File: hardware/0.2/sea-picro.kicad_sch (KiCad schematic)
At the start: 56 parts, among them J1 USB_C_Receptacle_USB2.0, J2 0.1" x 12, J3 0.1" x 12, Q1 FDG6335N, Q2 FDG6335N, SW1 RESET, U1 AP2112K-3.3, U3 W25Q128JVPIQ, U4 RP2040, Y1 12MHz

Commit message: 0.2 ready for review
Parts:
- added LOGO2: Sea-Picro, josh-logos:sea-picro-silk, symbol Graphic:SYM_LASER_Small
- added R6: 5K1, Resistor_SMD:R_0402_1005Metric, symbol Device:R
- C1, C10, C11, C12, C13, C14, C15, C16, C17, C18, C2, C3, C4, C8, C9, R1, R11, R12, R15, R2, R3, R4, R5, R9: JLC Basic (none) -> Y
- C19, C5: JLC Basic (none) -> Y; LCSC (none) -> C23733; MPN  (none) -> CL05A475MP5NRNC; Manufacturer (none) -> Samsung Electro-Mechanics
- C6, C7: JLC Basic (none) -> Y; LCSC C14445 -> C1548; MPN  CL05A105KP5NNNC -> 0402CG150J500NT; Manufacturer Samsung Electro-Mechanics -> FH(Guangdong Fenghua Advanced Tech)
- D1: JLC Basic (none) -> N; LCSC C699102 -> C122854; Manufacturer Yangzhou Yangjie Elec Tech -> Shikues
- D2: JLC Basic (none) -> Y; LCSC C268294 -> C72041; MPN  OSK40603C1E -> 19-217/BHC-ZL1M2RY/3T; Manufacturer OptoSupplyr -> Everlight Elec
- D3, F1, J1, R7, R8: JLC Basic (none) -> N
- Q1, Q2: value FDG6335N -> 2N7002DW-7-F; JLC Basic (none) -> N; LCSC (none) -> C83571; MPN  (none) -> 2N7002DW-7-F; Manufacturer (none) -> Diodes Incorporated
- R10: value 10K -> 5K1; JLC Basic (none) -> Y
- R13: JLC Basic (none) -> Y; LCSC (none) -> C25794; MPN  (none) -> 0402WGF5102TCE; Manufacturer (none) -> UNI-ROYAL(Uniroyal Elec)
- R14: JLC Basic (none) -> Y; LCSC (none) -> C25905; MPN  (none) -> 0402WGF5101TCE; Manufacturer (none) -> UNI-ROYAL(Uniroyal Elec)
- SW1: JLC Basic (none) -> N; LCSC (none) -> C913778; MPN  (none) -> 1TS026A-1000-0550-CT; Manufacturer (none) -> HYP (Hongyuan Precision)
- U1: value AP2112K-3.3 -> ME6211C33M5G-N; JLC Basic (none) -> N; LCSC C51118 -> C82942; MPN  AP2112K-3.3TRG1 -> ME6211C33M5G-N; Manufacturer Diodes Incorporated -> MICRONE(Nanjing Micro One Elec)
- U2: renamed from U3; value W25Q128JVPIQ -> GD25Q64CWIGR; JLC Basic (none) -> N; LCSC C190862 -> C395511; MPN  W25Q128JVPIQ -> GD25Q64CWIGR; Manufacturer Winbond Elec -> GigaDevice
- U3: renamed from U4; JLC Basic (none) -> N
- Y1: JLC Basic (none) -> Y; LCSC (none) -> C9002; MPN  (none) -> X322512MSB4SI; Manufacturer (none) -> Yangxing Tech
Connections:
- net +3V3: now also R6.1; no longer R10.1
- new net: R10.1, R6.2
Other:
- note added: "Q1A - inverter, as button can only pull to ground due to being backwards compatiable"
- note added: "Q1B - using body diode due to lack of space. Can sub with normal diode"
- note added: "Q2A - pulls nRST to GND"
- note removed: "Q1A - inverter, as button can only pull to ground"
- note removed: "Q1B - pulls nRST to GND"
- note removed: "Q2A - using body diode due to lack of space. Can sub with normal diode"

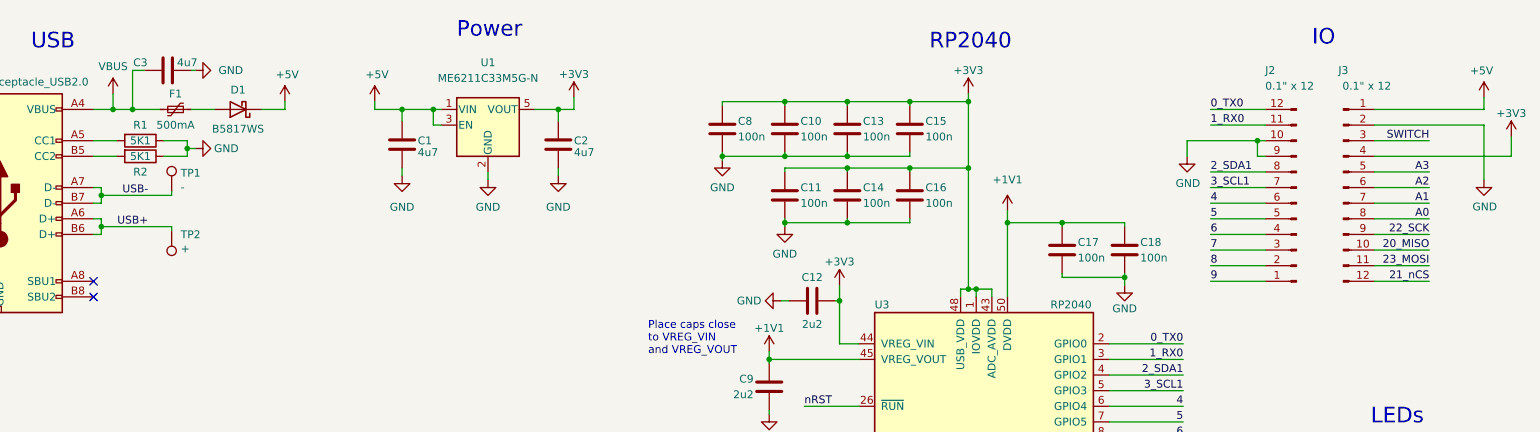
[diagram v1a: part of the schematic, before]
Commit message: add USB D+- on pin header
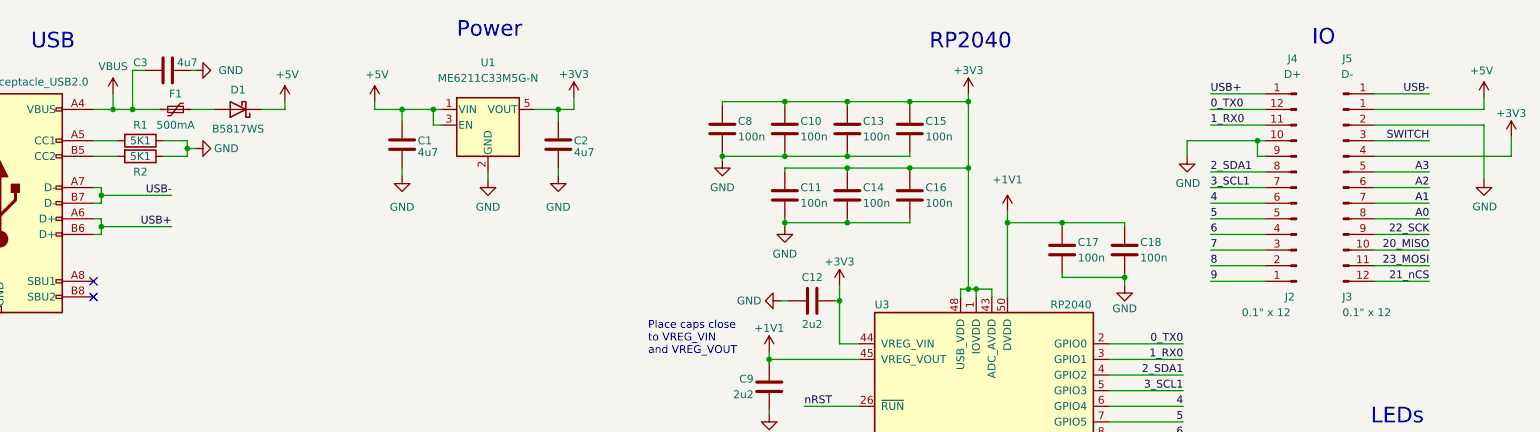
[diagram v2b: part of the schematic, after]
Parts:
- removed TP1: -, TestPoint:TestPoint_Pad_D1.0mm, symbol Connector:TestPoint
- removed TP2: +, TestPoint:TestPoint_Pad_D1.0mm, symbol Connector:TestPoint
- added J4: D+, josh-connectors:PinHeader_1x01_Circle, symbol Connector:Conn_01x01_Male
- added J5: D-, josh-connectors:PinHeader_1x01_Circle, symbol Connector:Conn_01x01_Male
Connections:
- net USB+: now also J4.1 (Pin_1)
- net USB-: now also J5.1 (Pin_1)
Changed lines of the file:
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@@
     (stroke (width 0) (type default) (color 0 0 0 0))
   )
+  (wire (pts (xy 231.14 28.575) (xy 240.03 28.575))
+    (stroke (width 0) (type default) (color 0 0 0 0))
+  )
   (wire (pts (xy 231.14 43.815) (xy 240.03 43.815))
     (stroke (width 0) (type default) (color 0 0 0 0))
@@
     (stroke (width 0) (type default) (color 0 0 0 0))
   )
-  (wire (pts (xy 62.23 44.45) (xy 62.23 45.085))
-    (stroke (width 0) (type default) (color 0 0 0 0))
-  )
   (wire (pts (xy 22.86 185.42) (xy 24.765 185.42))
     (stroke (width 0) (type default) (color 0 0 0 0))
@@
     (stroke (width 0) (type default) (color 0 0 0 0))
   )
+  (wire (pts (xy 257.81 28.575) (xy 266.7 28.575))
+    (stroke (width 0) (type default) (color 0 0 0 0))
+  )
   (wire (pts (xy 114.3 168.275) (xy 121.92 168.275))
     (stroke (width 0) (type default) (color 0 0 0 0))
@@
     (stroke (width 0) (type default) (color 0 0 0 0))
   )
-  (wire (pts (xy 62.23 50.8) (xy 62.23 50.165))
-    (stroke (width 0) (type default) (color 0 0 0 0))
-  )
   (wire (pts (xy 170.815 59.69) (xy 170.815 62.23))
     (stroke (width 0) (type default) (color 0 0 0 0))
@@
     (effects (font (size 1.27 1.27)) (justify right bottom))
   )
-  (label "USB-" (at 58.42 45.085 180)
+  (label "USB-" (at 62.23 45.085 180)
     (effects (font (size 1.27 1.27)) (justify right bottom))
   )
@@
     (effects (font (size 1.27 1.27)) (justify left bottom))
   )
+  (label "USB-" (at 266.7 28.575 180)
+    (effects (font (size 1.27 1.27)) (justify right bottom))
+  )
   (label "2_SDA1" (at 231.14 41.275 0)
     (effects (font (size 1.27 1.27)) (justify left bottom))
@@
     (effects (font (size 1.27 1.27)) (justify left bottom))
   )
+  (label "USB+" (at 231.14 28.575 0)
+    (effects (font (size 1.27 1.27)) (justify left bottom))
+  )
   (label "22_SCK" (at 266.7 51.435 180)
     (effects (font (size 1.27 1.27)) (justify right bottom))
@@
     (effects (font (size 1.27 1.27)) (justify left bottom))
   )
-  (label "USB+" (at 58.42 50.165 180)
+  (label "USB+" (at 62.23 50.165 180)
     (effects (font (size 1.27 1.27)) (justify right bottom))
   )
@@
   (symbol (lib_id "Connector:Conn_01x12_Male") (at 245.11 46.355 180) (unit 1)
     (in_bom no) (on_board yes)
-    (property "Reference" "J2" (id 0) (at 240.03 24.765 0)
+    (property "Reference" "J2" (id 0) (at 243.205 61.595 0)
       (effects (font (size 1.27 1.27)) (justify right))
     )
-    (property "Value" "0.1\" x 12" (id 1) (at 240.03 27.305 0)
+    (property "Value" "0.1\" x 12" (id 1) (at 236.22 64.135 0)
       (effects (font (size 1.27 1.27)) (justify right))
     )
@@
   (symbol (lib_id "Connector:Conn_01x12_Male") (at 252.73 43.815 0) (unit 1)
     (in_bom no) (on_board yes)
-    (property "Reference" "J3" (id 0) (at 252.73 24.765 0))
-    (property "Value" "0.1\" x 12" (id 1) (at 256.54 27.305 0))
+    (property "Reference" "J3" (id 0) (at 253.365 61.595 0))
+    (property "Value" "0.1\" x 12" (id 1) (at 256.54 64.135 0))
     (property "Footprint" "josh-connectors:Castellated_Short_P2.54x12" (id 2) (at 252.73 43.815 0)
       (effects (font (size 1.27 1.27)) hide)
@@
     )
   )
-  (symbol (lib_id "Connector:TestPoint") (at 62.23 44.45 0) (unit 1)
-    (in_bom no) (on_board yes)
-    (property "Reference" "TP1" (id 0) (at 63.7032 41.4528 0)
-      (effects (font (size 1.27 1.27)) (justify left))
-    )
-    (property "Value" "-" (id 1) (at 63.7032 43.7642 0)
-      (effects (font (size 1.27 1.27)) (justify left))
-    )
-    (property "Footprint" "TestPoint:TestPoint_Pad_D1.0mm" (id 2) (at 67.31 44.45 0)
-      (effects (font (size 1.27 1.27)) hide)
-    )
-    (property "Datasheet" "~" (id 3) (at 67.31 44.45 0)
-      (effects (font (size 1.27 1.27)) hide)
-    )
-    (property "DNP" "DNP" (id 4) (at 62.23 44.45 0)
-      (effects (font (size 1.27 1.27)) hide)
-    )
-    (pin "1")
-  )
-  (symbol (lib_id "Connector:TestPoint") (at 62.23 50.8 180) (unit 1)
-    (in_bom no) (on_board yes)
-    (property "Reference" "TP2" (id 0) (at 63.7032 51.4604 0)
-      (effects (font (size 1.27 1.27)) (justify right))
-    )
-    (property "Value" "+" (id 1) (at 63.7032 53.7718 0)
-      (effects (font (size 1.27 1.27)) (justify right))
-    )
-    (property "Footprint" "TestPoint:TestPoint_Pad_D1.0mm" (id 2) (at 57.15 50.8 0)
-      (effects (font (size 1.27 1.27)) hide)
-    )
-    (property "Datasheet" "~" (id 3) (at 57.15 50.8 0)
-      (effects (font (size 1.27 1.27)) hide)
-    )
-    (property "DNP" "DNP" (id 4) (at 62.23 50.8 0)
-      (effects (font (size 1.27 1.27)) hide)
-    )
-    (pin "1")
-  )
   (symbol (lib_id "Device:C") (at 159.385 76.2 0) (mirror y) (unit 1)
     (in_bom yes) (on_board yes)
@@
     (pin "2")
   )
+  (symbol (lib_id "Connector:Conn_01x01_Male") (at 245.11 28.575 180) (unit 1)
+    (in_bom yes) (on_board yes) (fields_autoplaced)
+    (property "Reference" "J4" (id 0) (at 244.475 22.86 0))
+    (property "Value" "D+" (id 1) (at 244.475 25.4 0))
+    (property "Footprint" "josh-connectors:PinHeader_1x01_Circle" (id 2) (at 245.11 28.575 0)
+      (effects (font (size 1.27 1.27)) hide)
+    )
+    (property "Datasheet" "~" (id 3) (at 245.11 28.575 0)
+      (effects (font (size 1.27 1.27)) hide)
+    )
+    (pin "1")
+  )
   (symbol (lib_id "power:+1V1") (at 159.385 70.485 0) (unit 1)
     (in_bom yes) (on_board yes)
@@
     (pin "1")
   )
+  (symbol (lib_id "Connector:Conn_01x01_Male") (at 252.73 28.575 0) (unit 1)
+    (in_bom yes) (on_board yes) (fields_autoplaced)
+    (property "Reference" "J5" (id 0) (at 253.365 22.86 0))
+    (property "Value" "D-" (id 1) (at 253.365 25.4 0))
+    (property "Footprint" "josh-connectors:PinHeader_1x01_Circle" (id 2) (at 252.73 28.575 0)
+      (effects (font (size 1.27 1.27)) hide)
+    )
+    (property "Datasheet" "~" (id 3) (at 252.73 28.575 0)
+      (effects (font (size 1.27 1.27)) hide)
+    )
+    (pin "1")
+  )
   (symbol (lib_id "Connector:TestPoint") (at 166.37 118.745 90) (unit 1)
     (in_bom no) (on_board yes)
@@
       (reference "J3") (unit 1) (value "0.1\" x 12") (footprint "josh-connectors:Castellated_Short_P2.54x12")
     )
+    (path "/6c8fe750-f5d5-45e3-8031-75f1034c352b"
+      (reference "J4") (unit 1) (value "D+") (footprint "josh-connectors:PinHeader_1x01_Circle")
+    )
+    (path "/8c9c179f-318f-4b3c-a530-90beee2229b8"
+      (reference "J5") (unit 1) (value "D-") (footprint "josh-connectors:PinHeader_1x01_Circle")
+    )
     (path "/00000000-0000-0000-0000-00005fd53dba"
       (reference "LOGO1") (unit 1) (value "Logo_Open_Hardware_Small") (footprint "josh-logos:OSHW_Logo_3.6x3.6_F.Mask")
@@
       (reference "SW1") (unit 1) (value "RESET") (footprint "josh-buttons-switches:SW_Push_1P1T_NO_HYP_1TS026A-1000-0550-CT")
     )
-    (path "/00000000-0000-0000-0000-0000608ed593"
-      (reference "TP1") (unit 1) (value "-") (footprint "TestPoint:TestPoint_Pad_D1.0mm")
-    )
-    (path "/00000000-0000-0000-0000-0000608f57b3"
-      (reference "TP2") (unit 1) (value "+") (footprint "TestPoint:TestPoint_Pad_D1.0mm")
-    )
     (path "/1e752a8f-58c3-4284-9f1d-9ed89d1dc919"
